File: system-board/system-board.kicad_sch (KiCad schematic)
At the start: 15 parts, among them J1 Micro_SD_Card_Det2, J2 Conn_01x02_Socket, J3 Conn_01x02_Socket, J4 BTN_SOCKET, J5 QWIIC, Q1 IRLB8721, U1 MAX98357AETE+T

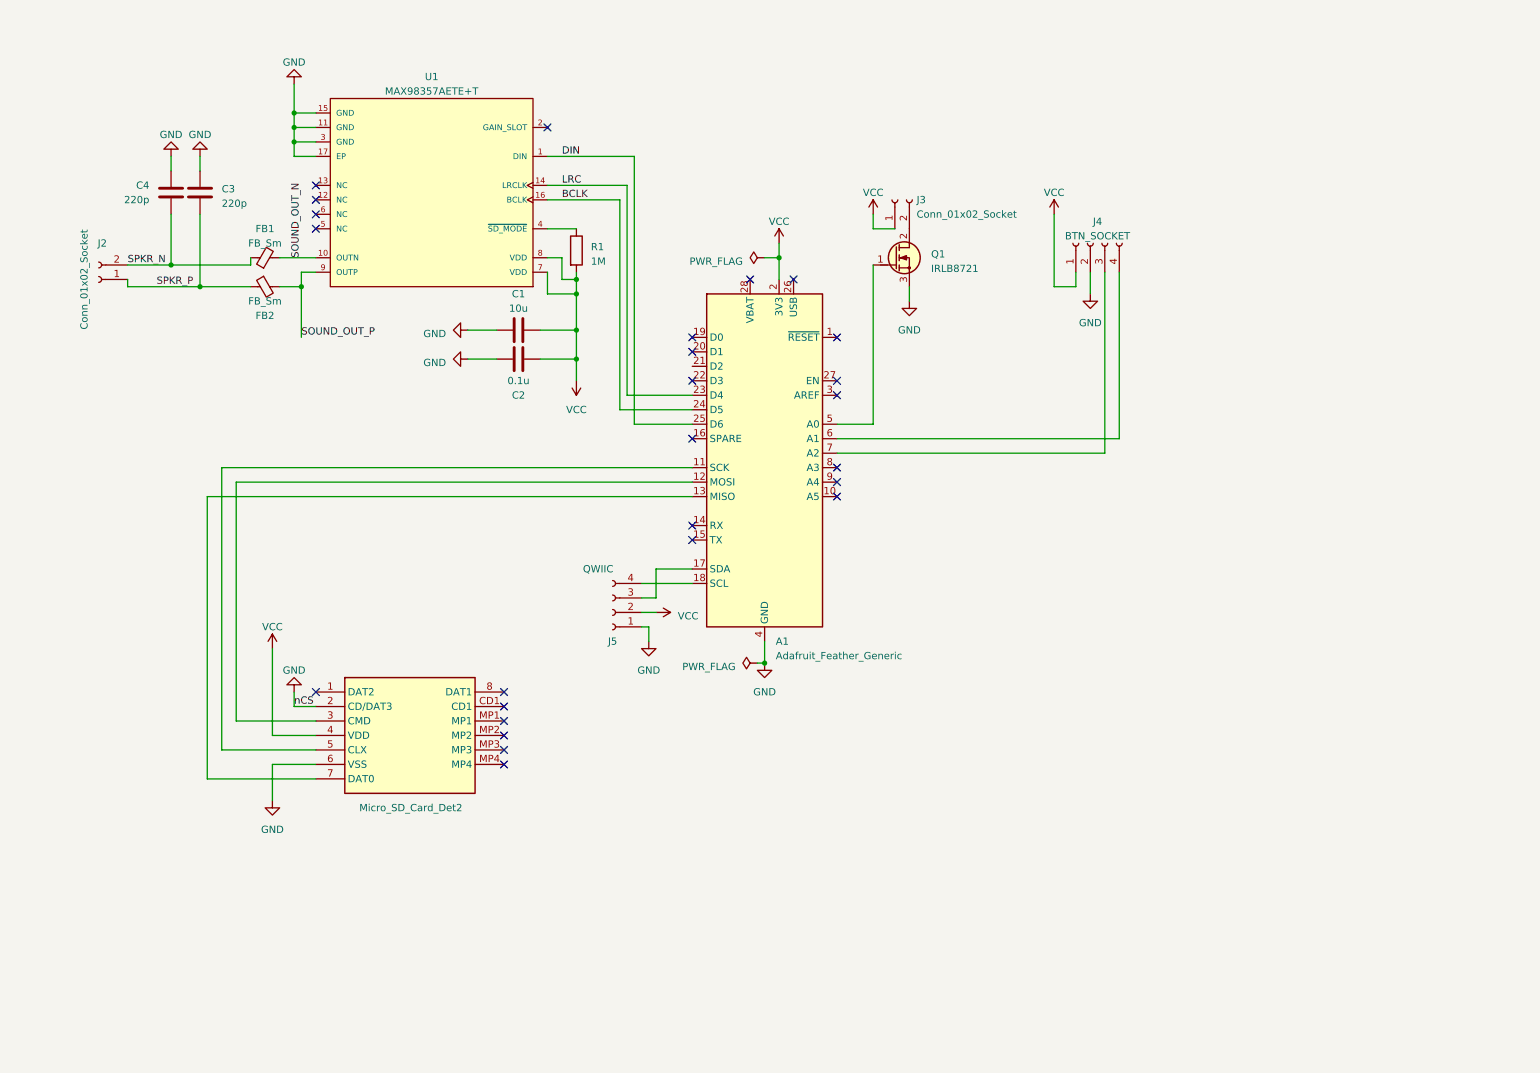
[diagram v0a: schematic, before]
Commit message: Do some calculations, overhaul system-board to be a single board, not a Feather add-on.
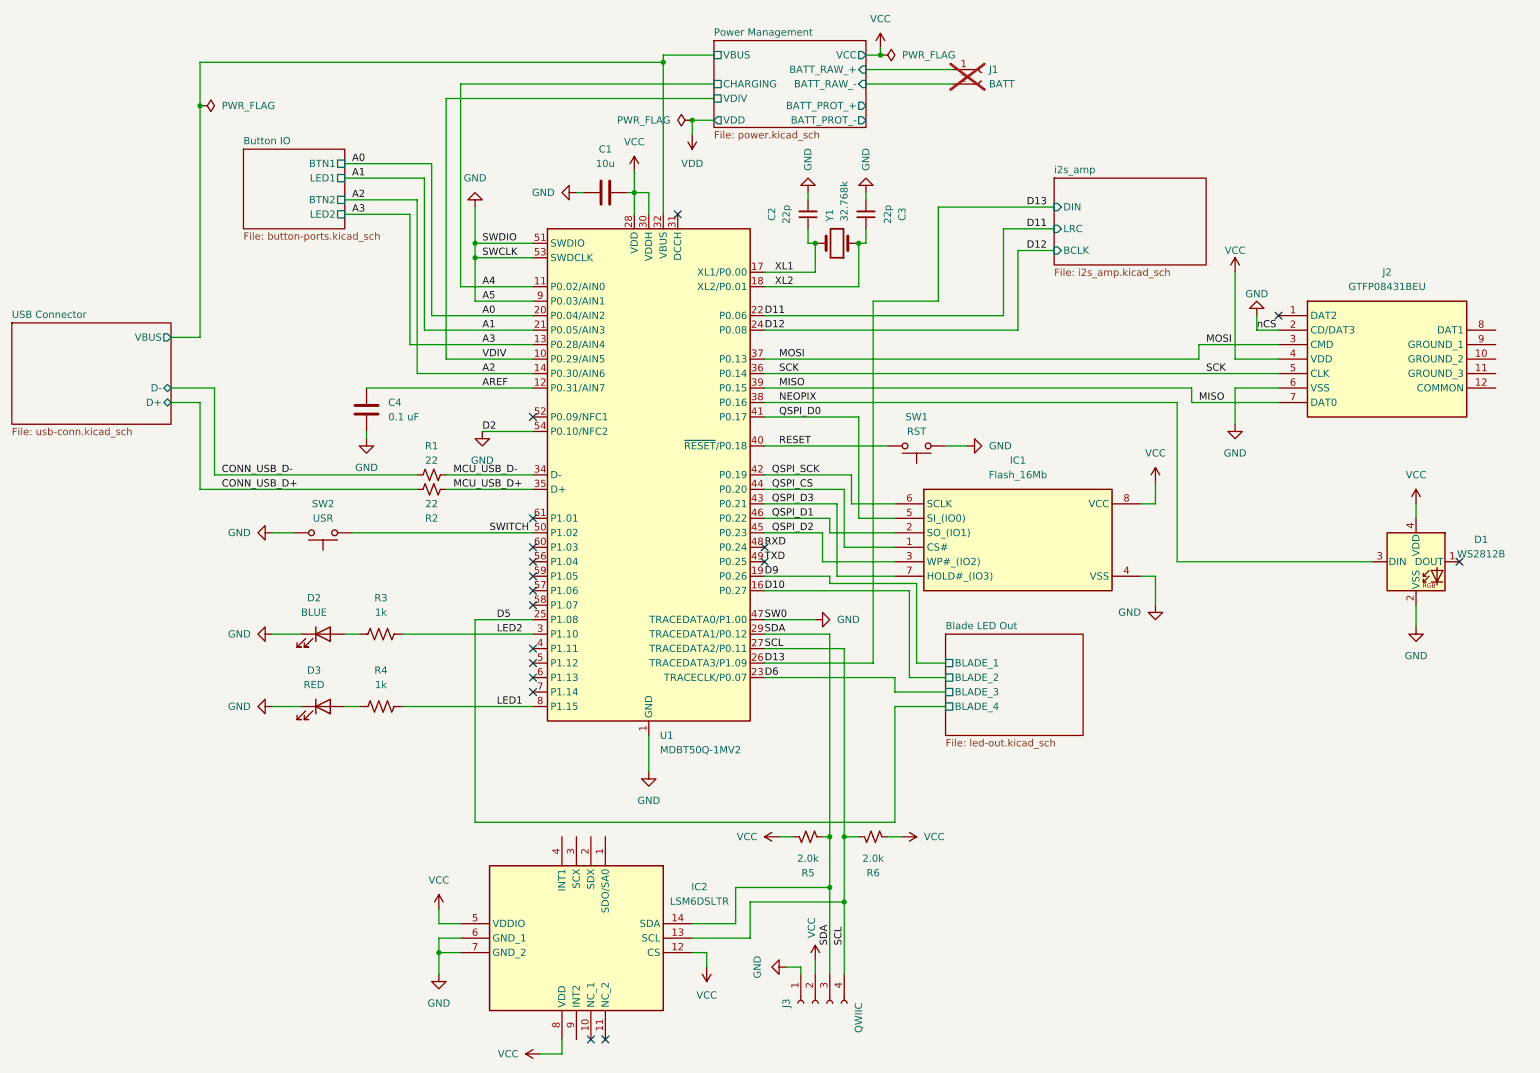
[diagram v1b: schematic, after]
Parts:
- removed A1: Adafruit_Feather_Generic, Module:Adafruit_Feather_WithMountingHoles, symbol MCU_Module:Adafruit_Feather_Generic
- removed C2: 0.1u, Capacitor_SMD:C_0603_1608Metric, symbol Device:C
- removed C3: 220p, Capacitor_SMD:C_0402_1005Metric, symbol Device:C
- removed FB1, FB2: FB_Sm, PCM_Ferrite_SMD_AKL:Ferrite_0603_1608Metric, symbol Device:FerriteBead_Small
- removed J1: Micro_SD_Card_Det2, TF115, symbol TF-115:TF-115
- removed J2, J3: Conn_01x02_Socket, Connector_JST:JST_PH_S2B-PH-K_1x02_P2.00mm_Horizontal, symbol Connector:Conn_01x02_Socket
- removed J4: BTN_SOCKET, Connector_JST:JST_PH_S4B-PH-SM4-TB_1x04-1MP_P2.00mm_Horizontal, symbol Connector:Conn_01x04_Socket
- removed J5: QWIIC, Connector_JST:JST_SH_SM04B-SRSS-TB_1x04-1MP_P1.00mm_Horizontal, symbol Connector:Conn_01x04_Socket
- removed Q1: IRLB8721, Package_TO_SOT_THT:TO-220-3_Horizontal_TabDown, symbol PCM_Transistor_MOSFET_AKL:IRLB8721
- removed R1: 1M, Resistor_SMD:R_1206_3216Metric, symbol Device:R
- removed U1: MAX98357AETE+T, MaximCustom:Maxim_Integrated-T1633-4-0-V-IPC_C, symbol Amplifier_Audio:MAX98357AETE+T
- added C2, C3: 22p, Capacitor_SMD:C_0402_1005Metric, symbol Device:C_Small
- added D1: WS2812B, Imports:WS2812B-2020, symbol LED:WS2812B
- added D2: BLUE, LED_SMD:LED_0603_1608Metric, symbol Device:LED
- added D3: RED, LED_SMD:LED_0603_1608Metric, symbol Device:LED
- added IC1: Flash_16Mb, Imports:USON-8-03x02mm-PSON50P200X300X50-9N, symbol imports-new:GD25Q16ETIGR
- added IC2: LSM6DSLTR, Imports:LSM6DSLTR, symbol imports:LSM6DSLTR
- added J1: BATT, Connector_PinSocket_2.00mm:PinSocket_1x02_P2.00mm_Vertical, symbol Connector:Conn_01x02_Socket
- added J2: GTFP08431BEU, Imports:GTFP08431BEU, symbol imports:GTFP08431BEU
- added J3: QWIIC, Connector_JST:JST_SH_SM04B-SRSS-TB_1x04-1MP_P1.00mm_Horizontal, symbol Connector:Conn_01x04_Socket
- added R1, R2: 22, Resistor_SMD:R_0402_1005Metric, symbol Device:R_Small_US
- added R3, R4: 1k, Resistor_SMD:R_0402_1005Metric, symbol Device:R_US
- added R5, R6: 2.0k, Resistor_SMD:R_0402_1005Metric, symbol Device:R_Small_US
- added SW1: RST, Imports:CK_Components-KMR231NG_LFS-MFG, symbol Switch:SW_Push
- added SW2: USR, Imports:CK_Components-KMR231NG_LFS-MFG, symbol Switch:SW_Push
- added U1: MDBT50Q-1MV2, Imports:XCVR_MDBT50Q-1MV2, symbol RF_Module:MDBT50Q-1MV2
- added Y1: 32.768k, Imports:XTAL_ECS-.327-12.5-1210B-N-TR, symbol Device:Crystal
- C1: footprint Capacitor_SMD:C_1206_3216Metric -> Capacitor_SMD:C_0402_1005Metric; JLCPCB Part # C13585 -> C723895; Manufacturer (none) -> Murata; Manufacturer_Part_Number (none) -> GRM155R60J106ME05D; Mouser Part Number (none) -> 81-GRM155R60J106M05D; Substitution Comments Keep the value correct. -> (none)
- C4: value 220p -> 0.1 uF; footprint Capacitor_SMD:C_0402_1005Metric -> Capacitor_SMD:C_0805_2012Metric; JLCPCB Part # C1530 -> C3018562; Manufacturer (none) -> KEMET; Manufacturer_Part_Number (none) -> C0805C104K5RACTU; Mouser Part Number (none) -> 80-C0805C104K5R; Substitution Comments Keep the value correct. -> (none)
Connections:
- net GND: now also C2.2, C3.2, D1.2 (VSS), D2.1 (K), D3.1 (K), IC1.4 (VSS), IC2.6 (GND_1), IC2.7 (GND_2), J2.2 (CD/DAT3), J2.6 (VSS), J3.1 (Pin_1), SW1.1, SW2.1, U1.1 (GND), U1.15 (GND), U1.2 (GND), U1.33 (GND), U1.47 (TRACEDATA0/P1.00), U1.51 (SWDIO), U1.53 (SWDCLK), U1.54 (P0.10/NFC2), U1.55 (GND), U1.9 (P0.03/AIN1)
- net VCC: now also D1.4 (VDD), IC1.8 (VCC), IC2.12 (CS), IC2.5 (VDDIO), IC2.8 (VDD), J2.4 (VDD), J3.2 (Pin_2), R5.1, R6.2, U1.28 (VDD), U1.30 (VDDH)
- net SPKR_N renamed AREF
- net AREF: now also U1.12 (P0.31/AIN7)
- new net: D3.2 (A), R4.1
- new net: D2.2 (A), R3.1
- new net A0: U1.20 (P0.04/AIN2)
- new net A1: U1.21 (P0.05/AIN3)
- new net A2: U1.14 (P0.30/AIN6)
- new net A3: U1.13 (P0.28/AIN4)
- new net A4: U1.11 (P0.02/AIN0)
- new net CONN_USB_D+: R2.1
- new net CONN_USB_D-: R1.1
- new net D10: U1.16 (P0.27)
- new net D11: U1.22 (P0.06)
- new net D12: U1.24 (P0.08)
- new net D13: U1.26 (TRACEDATA3/P1.09)
- new net D5: U1.25 (P1.08)
- new net D6: U1.23 (TRACECLK/P0.07)
- new net D9: U1.19 (P0.26)
- new net LED1: R4.2, U1.8 (P1.15)
- new net LED2: R3.2, U1.3 (P1.10)
- new net MCU_USB_D+: R2.2, U1.35 (D+)
- new net MCU_USB_D-: R1.2, U1.34 (D-)
- new net MISO: J2.7 (DAT0), U1.39 (P0.15)
- new net MOSI: J2.3 (CMD), U1.37 (P0.13)
- new net NEOPIX: D1.3 (DIN), U1.38 (P0.16)
- new net Power Management/BATT_RAW_+: J1.1 (Pin_1)
- new net Power Management/BATT_RAW_-: J1.2 (Pin_2)
- new net Power Management/VBUS: U1.32 (VBUS)
- new net QSPI_CS: IC1.1 (CS#), U1.44 (P0.20)
- new net QSPI_D0: IC1.5 (SI_(IO0)), U1.41 (P0.17)
- new net QSPI_D1: IC1.2 (SO_(IO1)), U1.46 (P0.22)
- new net QSPI_D2: IC1.3 (WP#_(IO2)), U1.45 (P0.23)
- new net QSPI_D3: IC1.7 (HOLD#_(IO3)), U1.43 (P0.21)
- new net QSPI_SCK: IC1.6 (SCLK), U1.42 (P0.19)
- new net RESET: SW1.2, U1.40 (~{RESET}/P0.18)
- new net RXD: U1.48 (P0.24)
- new net SCK: J2.5 (CLK), U1.36 (P0.14)
- new net SCL: IC2.13 (SCL), J3.4 (Pin_4), R6.1, U1.27 (TRACEDATA2/P0.11)
- new net SDA: IC2.14 (SDA), J3.3 (Pin_3), R5.2, U1.29 (TRACEDATA1/P0.12)
- new net SWITCH: SW2.2, U1.50 (P1.02)
- new net TXD: U1.49 (P0.25)
- new net VDIV: U1.10 (P0.29/AIN5)
- new net XL1: C2.1, U1.17 (XL1/P0.00), Y1.2
- new net XL2: C3.1, U1.18 (XL2/P0.01), Y1.1
- no-connect marks 26 -> 18
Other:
- added sheet Blade LED Out (led-out.kicad_sch)
- added sheet Button IO (button-ports.kicad_sch)
- added sheet Power Management (power.kicad_sch)
- added sheet USB Connector (usb-conn.kicad_sch)
- added sheet i2s_amp (i2s_amp.kicad_sch)

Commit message: Add imported footprints & models
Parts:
- D1: value WS2812B -> WS2812B-2020
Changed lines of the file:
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@@
       (effects (font (size 1.27 1.27)))
     )
-    (property "Value" "WS2812B" (at 271.78 107.8739 0)
+    (property "Value" "WS2812B-2020" (at 271.78 107.8739 0)
       (effects (font (size 1.27 1.27)))
     )

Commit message: First attempt
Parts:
- removed J2: GTFP08431BEU, Imports:GTFP08431BEU, symbol imports:GTFP08431BEU
- added J11: 503398-1892, Imports:Molex uSD Card Holder Push-Push 503398-1892, symbol imports:503398-1892
- J1: now left out of the parts list
- J3: JLCPCB Part # (none) -> C160404; Manufacturer (none) -> JST Sales America, Inc; Manufacturer_Part_Number (none) -> SM04B-SRSS-TB(LF)(SN); digikey part number (none) -> 455-1804-6-ND
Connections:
- net GND: now also J11.2 (CD/DAT3), J11.6 (VSS)
- net MISO: now also J11.7 (DAT0)
- net MOSI: now also J11.3 (CMD)
- net SCK: now also J11.5 (CLK)
- net VCC: now also J11.4 (VDD)
- no-connect marks 18 -> 26

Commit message: Redo system-board PCB to use fewer connectors
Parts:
- C1: digikey part number (none) -> 490-GRM155R60J106ME05DTR-ND
- C2, C3: digikey part number (none) -> 490-GCM1555G1H220JA16DTR-ND
- C4: digikey part number (none) -> 399-C0805C104K5RAC7800TR-ND
- D2: digikey part number (none) -> 160-1827-2-ND
- D3: digikey part number (none) -> 160-1830-2-ND
- IC1: digikey part number (none) -> 1970-GD25Q16EEIGRTR-ND
- IC2: digikey part number (none) -> 497-16705-2-ND
- J11: digikey part number (none) -> WM11190TR-ND
- R1, R2: digikey part number (none) -> 311-22.0LRTR-ND
- R3, R4: digikey part number (none) -> A121534TR-ND
- R5, R6: digikey part number (none) -> 311-2.0KJRTR-ND
- SW1, SW2: digikey part number (none) -> CKN10246TR-ND
- U1: Manufacturer (none) -> Raytac; Manufacturer_Part_Number (none) -> MDBT50Q-1MV2; Mouser Part Number (none) -> 485-4078; digikey part number (none) -> 3271-MDBT50Q-1MV2-ND
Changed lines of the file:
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@@
+      (effects (font (size 1.27 1.27)) hide)
+    )
+    (property "digikey part number" "CKN10246TR-ND" (at 172.72 88.9 0)
       (effects (font (size 1.27 1.27)) hide)
     )
@@
     )
     (property "Manufacturer" "MOLEX" (at 236.22 66.04 0)
+      (effects (font (size 1.27 1.27)) hide)
+    )
+    (property "digikey part number" "WM11190TR-ND" (at 236.22 66.04 0)
       (effects (font (size 1.27 1.27)) hide)
     )
@@
       (effects (font (size 1.27 1.27)) hide)
     )
+    (property "digikey part number" "CKN10246TR-ND" (at 68.58 104.14 0)
+      (effects (font (size 1.27 1.27)) hide)
+    )
     (pin "1")
     (pin "2")
@@
     )
     (property "Mouser Part Number" "81-GRM155R60J106M05D" (at 118.11 44.45 0)
+      (effects (font (size 1.27 1.27)) hide)
+    )
+    (property "digikey part number" "490-GRM155R60J106ME05DTR-ND" (at 118.11 44.45 0)
       (effects (font (size 1.27 1.27)) hide)
     )
@@
       (effects (font (size 1.27 1.27)) hide)
     )
+    (property "digikey part number" "160-1830-2-ND" (at 68.58 134.62 0)
+      (effects (font (size 1.27 1.27)) hide)
+    )
     (pin "1")
     (pin "2")
@@
       (effects (font (size 1.27 1.27)) hide)
     )
+    (property "digikey part number" "490-GCM1555G1H220JA16DTR-ND" (at 163.83 48.26 0)
+      (effects (font (size 1.27 1.27)) hide)
+    )
     (pin "1")
     (pin "2")
@@
     )
     (property "Mouser Part Number" "81-GCM1555G1H220JA6D" (at 153.67 48.26 0)
+      (effects (font (size 1.27 1.27)) hide)
+    )
+    (property "digikey part number" "490-GCM1555G1H220JA16DTR-ND" (at 153.67 48.26 0)
       (effects (font (size 1.27 1.27)) hide)
     )
@@
       (effects (font (size 1.27 1.27)) hide)
     )
+    (property "digikey part number" "311-2.0KJRTR-ND" (at 165.1 157.48 0)
+      (effects (font (size 1.27 1.27)) hide)
+    )
     (pin "1")
     (pin "2")
@@
       (effects (font (size 1.27 1.27)) hide)
     )
+    (property "digikey part number" "311-2.0KJRTR-ND" (at 153.67 157.48 0)
+      (effects (font (size 1.27 1.27)) hide)
+    )
     (pin "1")
     (pin "2")
@@
     )
     (property "Mouser Part Number" "279-CRG0402F1K0 " (at 78.74 134.62 0)
+      (effects (font (size 1.27 1.27)) hide)
+    )
+    (property "digikey part number" "A121534TR-ND" (at 78.74 134.62 0)
       (effects (font (size 1.27 1.27)) hide)
     )
@@
     )
     (property "Manufacturer" "GigaDevice Semicon Beijing" (at 168.91 99.06 0)
+      (effects (font (size 1.27 1.27)) hide)
+    )
+    (property "digikey part number" "1970-GD25Q16EEIGRTR-ND" (at 168.91 99.06 0)
       (effects (font (size 1.27 1.27)) hide)
     )
@@
       (effects (font (size 1.27 1.27)) hide)
     )
+    (property "digikey part number" "311-22.0LRTR-ND" (at 87.63 93.98 0)
+      (effects (font (size 1.27 1.27)) hide)
+    )
     (pin "1")
     (pin "2")
@@
       (effects (font (size 1.27 1.27)) hide)
     )
+    (property "digikey part number" "311-22.0LRTR-ND" (at 87.63 96.52 0)
+      (effects (font (size 1.27 1.27)) hide)
+    )
     (pin "1")
     (pin "2")
@@
     )
     (property "Manufacturer" "STMicroelectronics" (at 118.11 157.48 0)
+      (effects (font (size 1.27 1.27)) hide)
+    )
+    (property "digikey part number" "497-16705-2-ND" (at 118.11 157.48 0)
       (effects (font (size 1.27 1.27)) hide)
     )
@@
     )
     (property "Datasheet" "https://www.raytac.com/download/index.php?index_id=43" (at 125.73 99.06 0)
+      (effects (font (size 1.27 1.27)) hide)
+    )
+    (property "Manufacturer" "Raytac" (at 125.73 93.98 0)
+      (effects (font (size 1.27 1.27)) hide)
+    )
+    (property "Manufacturer_Part_Number" "MDBT50Q-1MV2" (at 125.73 93.98 0)
+      (effects (font (size 1.27 1.27)) hide)
+    )
+    (property "Mouser Part Number" "485-4078" (at 125.73 93.98 0)
+      (effects (font (size 1.27 1.27)) hide)
+    )
+    (property "digikey part number" "3271-MDBT50Q-1MV2-ND" (at 125.73 93.98 0)
       (effects (font (size 1.27 1.27)) hide)
     )
@@
       (effects (font (size 1.27 1.27)) hide)
     )
+    (property "digikey part number" "160-1827-2-ND" (at 68.58 121.92 0)
+      (effects (font (size 1.27 1.27)) hide)
+    )
     (pin "1")
     (pin "2")
@@
       (effects (font (size 1.27 1.27)) hide)
     )
+    (property "digikey part number" "399-C0805C104K5RAC7800TR-ND" (at 76.2 82.55 0)
+      (effects (font (size 1.27 1.27)) hide)
+    )
     (pin "1")
     (pin "2")
@@
       (effects (font (size 1.27 1.27)) hide)
     )
+    (property "digikey part number" "A121534TR-ND" (at 78.74 121.92 0)
+      (effects (font (size 1.27 1.27)) hide)
+    )

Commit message: Yet another PCB Revision
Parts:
- added J6: DBG, Imports:Prog-Pads, symbol Connector:Conn_01x05_Socket
- C1: MPN (none) -> GRM155R60J106ME05D; package (none) -> 0402
- C2, C3: MPN (none) -> GCM1555G1H220JA16D; package (none) -> 0402
- C4: MPN (none) -> C0805C104K5RACTU; package (none) -> 0805
- D1: MPN (none) -> WS2812B-2020; package (none) -> SMD,2x2mm
- D2: MPN (none) -> LTST-C193TBKT-5A; package (none) -> 0603
- D3: MPN (none) -> LTST-C193KRKT-5A; package (none) -> 0603
- IC1: Height 1.75 -> (none); MPN (none) -> GD25Q16EEIGR; Manufacturer_Name GigaDevice Semiconductor (HK) Limited -> (none); package (none) -> USON-8(2x3)
- IC2: Height 0.86 -> (none); MPN (none) -> LSM6DSLTR; Manufacturer_Name STMicroelectronics -> (none); package (none) -> LGA-14
- J11: MPN (none) -> 503398-1892; Manufacturer_Name Molex -> (none); package (none) -> SMD
- J3: MPN (none) -> SM04B-SRSS-TB(LF)(SN); package (none) -> --; now in the parts list
- R1, R2: MPN (none) -> RC0402FR-0722RL; package (none) -> 0402
- R3, R4: MPN (none) -> CRG0402F1K0; package (none) -> 0402
- R5, R6: MPN (none) -> RC0402JR-072KL; package (none) -> 0402
- SW1, SW2: MPN (none) -> KMR231NGLFS; package (none) -> SMD
- U1: MPN (none) -> MDBT50Q-1MV2; package (none) -> --
- Y1: MPN (none) -> ECS-.327-12.5-1210B-N-TR; digikey part number (none) -> XC2873TR-ND; package (none) -> SMD1210-4P
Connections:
- net GND: now also J6.4 (Pin_4); no longer U1.47 (TRACEDATA0/P1.00), U1.51 (SWDIO), U1.53 (SWDCLK)
- net VCC: now also J6.5 (Pin_5)
- new net SW0: J6.3 (Pin_3), U1.47 (TRACEDATA0/P1.00)
- new net SWCLK: J6.1 (Pin_1), U1.53 (SWDCLK)
- new net SWDIO: J6.2 (Pin_2), U1.51 (SWDIO)

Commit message: Redo design again
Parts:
- removed IC2: LSM6DSLTR, Imports:LSM6DSLTR, symbol imports:LSM6DSLTR
- removed J3: QWIIC, Connector_JST:JST_SH_SM04B-SRSS-TB_1x04-1MP_P1.00mm_Horizontal, symbol Connector:Conn_01x04_Socket
- removed R5, R6: 2.0k, Resistor_SMD:R_0402_1005Metric, symbol Device:R_Small_US
- IC1: footprint Imports:USON-8-03x02mm-PSON50P200X300X50-9N -> Package_SO:SOP-8_3.9x4.9mm_P1.27mm; JLCPCB Part # C2986331 -> C2904431; MPN GD25Q16EEIGR -> GD25Q16ETIGR; Manufacturer_Part_Number GD25Q16EEIGR -> GD25Q16ETIGR; Mouser Part Number 363-GD25Q16EEIGR -> 363-GD25Q16ETIGR; Mouser Price/Stock https://www.mouser.com/ProductDetail/GigaDevice/GD25Q16EEIG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 -> https://www.mouser.com/ProductDetail/GigaDevice/GD25Q16ETIG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; digikey part number 1970-GD25Q16EEIGRTR-ND -> --; package USON-8(2x3) -> SOP-8
- R1, R2: Mouser Part Number RC0402FR-0722RL -> 603-RC0402FR-0722RL
- renumbered J11 to J2, J6 to J3
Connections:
- no-connect marks 26 -> 19
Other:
- added sheet i2c_devices (i2c_devs.kicad_sch)
